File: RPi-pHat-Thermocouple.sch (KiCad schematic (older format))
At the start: 27 parts, among them J1 RPi_GPIO, P1 CONN_01X02, P2 CONN_01X02, P3 CONN_01X02, P4 CONN_01X02, P6 CONN_01X03, Q1 NUD3124, SW1 Write, U1 MAX31850K, U3 MAX31850K, U4 MAX31850K, U5 AT24CS32, U6 MAX31850K

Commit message: Updated schematic parts fields on MAX31850k parts.
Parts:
- U1, U3, U4, U6: Manufacturer (none) -> Maxim; Part Number (none) -> MAX31850KATB+; Vendor (none) -> Mouser; Vendor Part Number (none) -> 700-MAX31850KATB+
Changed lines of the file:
@@
 F 1 "MAX31850K" H 4050 2050 50  0000 L CNN
 F 2 "Housings_DFN_QFN_ML:TDFN-10-1EP_3x4mm_Pitch0.5mm" H 4000 1700 50  0001 C CIN
-F 3 "" H 4000 1700 50  0000 C CNN
+F 3 "https://datasheets.maximintegrated.com/en/ds/MAX31850-MAX31851.pdf" H 4000 1700 50  0001 C CNN
+F 4 "MAX31850KATB+" H 4000 1700 60  0001 C CNN "Part Number"
+F 5 "Maxim" H 4000 1700 60  0001 C CNN "Manufacturer"
+F 6 "Mouser" H 4000 1700 60  0001 C CNN "Vendor"
+F 7 "700-MAX31850KATB+" H 4000 1700 60  0001 C CNN "Vendor Part Number"
 	1    4000 1700
 	1    0    0    -1
@@
 F 1 "MAX31850K" H 4050 3750 50  0000 L CNN
 F 2 "Housings_DFN_QFN_ML:TDFN-10-1EP_3x4mm_Pitch0.5mm" H 4000 3400 50  0001 C CIN
-F 3 "" H 4000 3400 50  0000 C CNN
+F 3 "https://datasheets.maximintegrated.com/en/ds/MAX31850-MAX31851.pdf" H 4000 3400 50  0001 C CNN
+F 4 "MAX31850KATB+" H 4000 3400 60  0001 C CNN "Part Number"
+F 5 "Maxim" H 4000 3400 60  0001 C CNN "Manufacturer"
+F 6 "Mouser" H 4000 3400 60  0001 C CNN "Vendor"
+F 7 "700-MAX31850KATB+" H 4000 3400 60  0001 C CNN "Vendor Part Number"
 	1    4000 3400
 	1    0    0    -1
@@
 F 1 "MAX31850K" H 4050 5450 50  0000 L CNN
 F 2 "Housings_DFN_QFN_ML:TDFN-10-1EP_3x4mm_Pitch0.5mm" H 4000 5100 50  0001 C CIN
-F 3 "" H 4000 5100 50  0000 C CNN
+F 3 "https://datasheets.maximintegrated.com/en/ds/MAX31850-MAX31851.pdf" H 4000 5100 50  0001 C CNN
+F 4 "MAX31850KATB+" H 4000 5100 60  0001 C CNN "Part Number"
+F 5 "Maxim" H 4000 5100 60  0001 C CNN "Manufacturer"
+F 6 "Mouser" H 4000 5100 60  0001 C CNN "Vendor"
+F 7 "700-MAX31850KATB+" H 4000 5100 60  0001 C CNN "Vendor Part Number"
 	1    4000 5100
 	1    0    0    -1
@@
 F 1 "MAX31850K" H 4050 7150 50  0000 L CNN
 F 2 "Housings_DFN_QFN_ML:TDFN-10-1EP_3x4mm_Pitch0.5mm" H 4000 6800 50  0001 C CIN
-F 3 "" H 4000 6800 50  0000 C CNN
+F 3 "https://datasheets.maximintegrated.com/en/ds/MAX31850-MAX31851.pdf" H 4000 6800 50  0001 C CNN
+F 4 "MAX31850KATB+" H 4000 6800 60  0001 C CNN "Part Number"
+F 5 "Maxim" H 4000 6800 60  0001 C CNN "Manufacturer"
+F 6 "Mouser" H 4000 6800 60  0001 C CNN "Vendor"
+F 7 "700-MAX31850KATB+" H 4000 6800 60  0001 C CNN "Vendor Part Number"
 	1    4000 6800
 	1    0    0    -1
@@
 	7050 4000 7050 5450
 Wire Wire Line
-	7050 4000 9600 4000
+	9600 4000 7050 4000
 Wire Wire Line
 	3400 1200 3300 1200

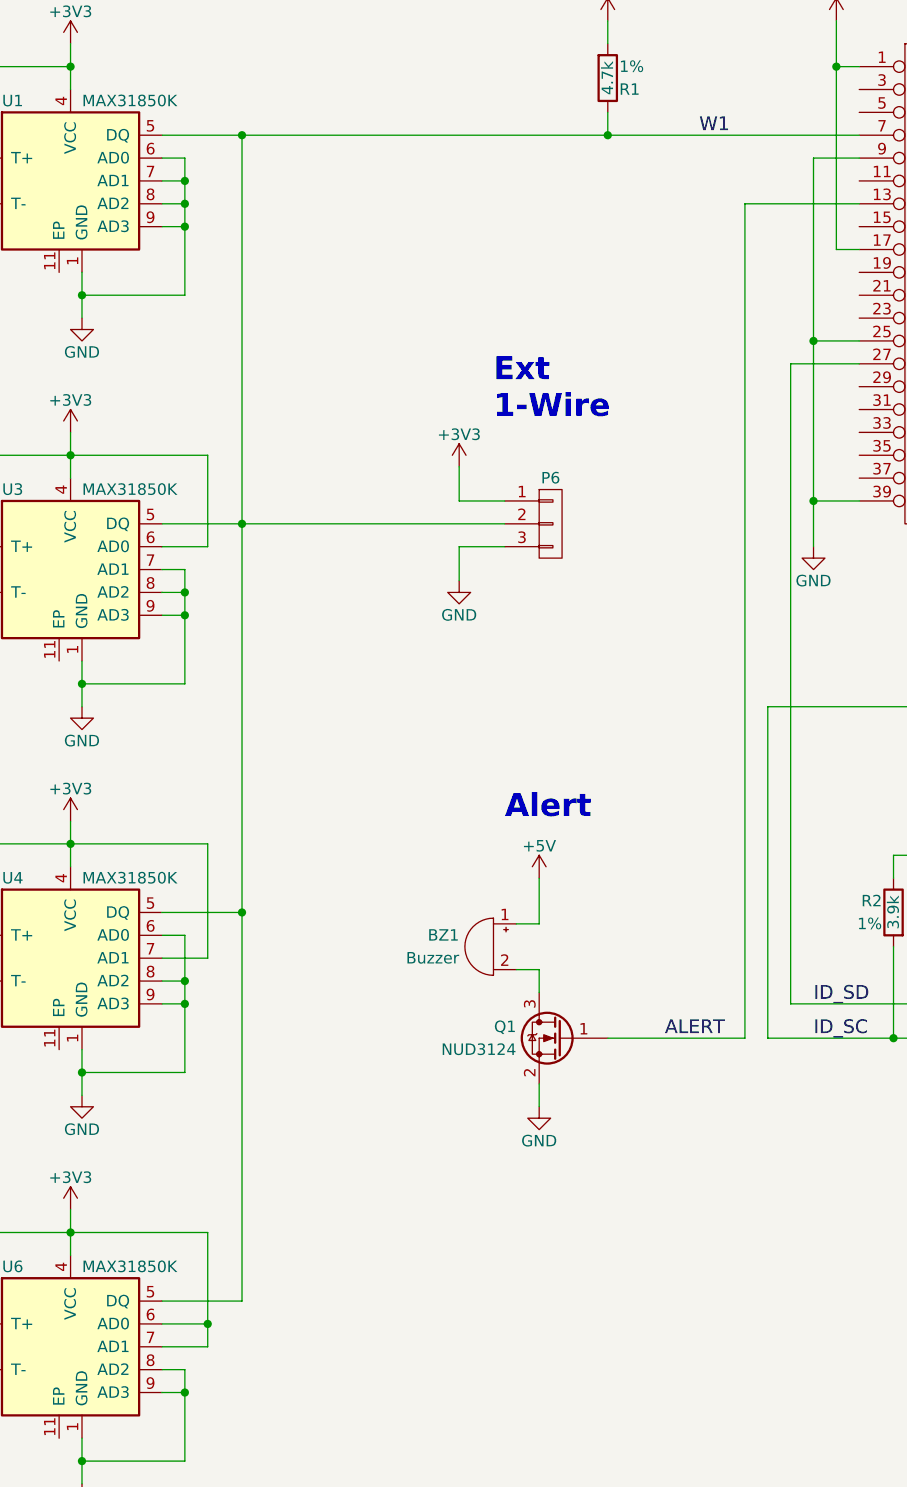
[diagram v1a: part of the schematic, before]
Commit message: Added U2 and R5
Fixed Alert sounding as soon as power is applied by adding pulldown
(R5). Added Ds18S20 (U2) so the Linux kernel will properly access the
MAX31850K.
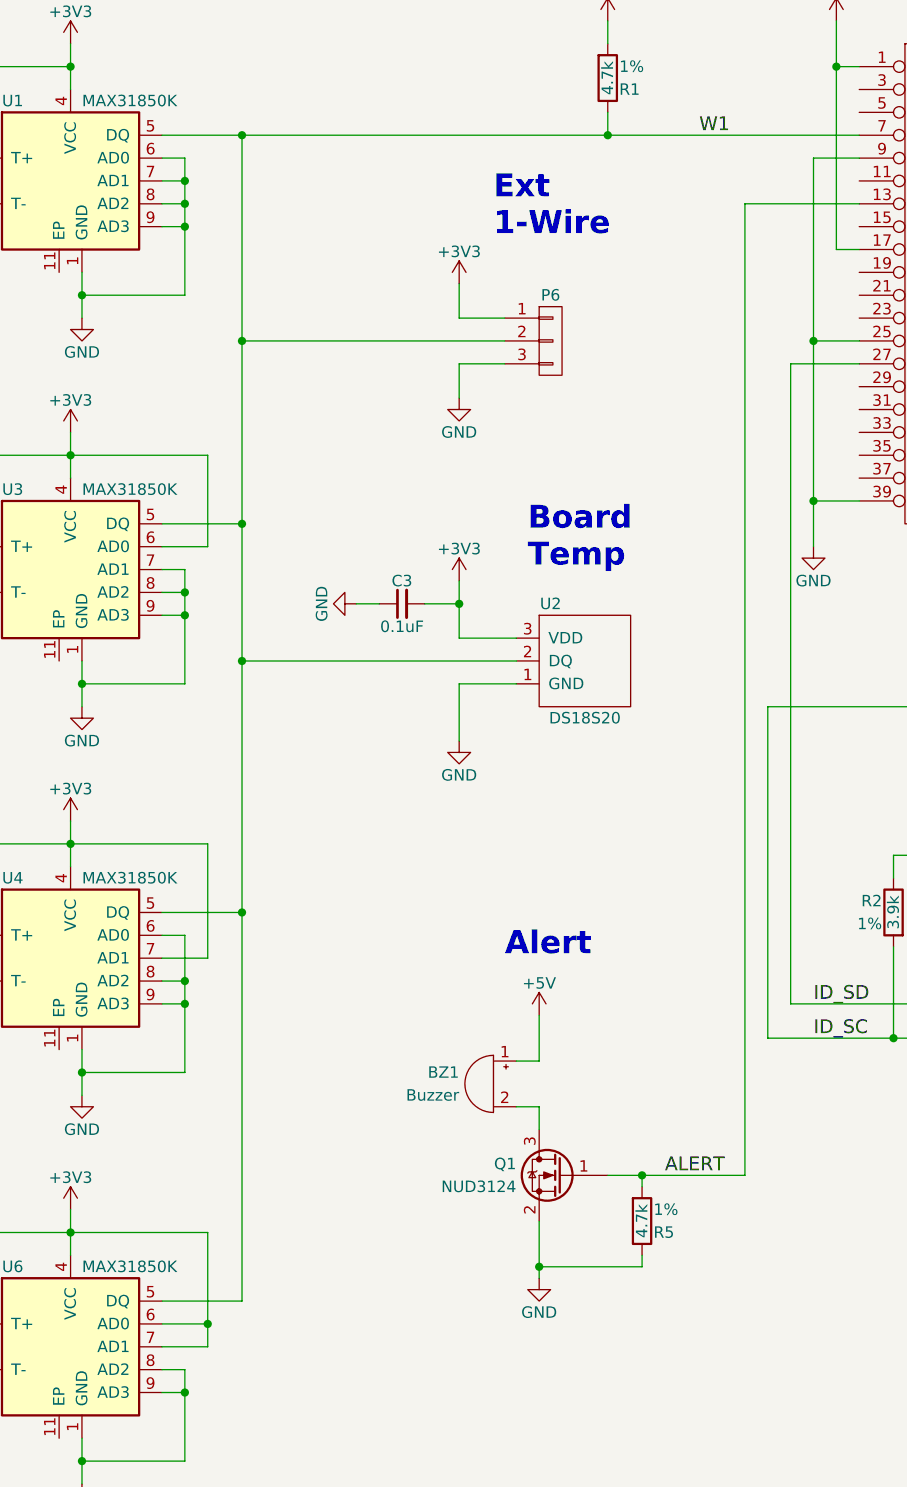
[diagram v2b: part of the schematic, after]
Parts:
- added C3: 0.1uF, Capacitors_SMD:C_0603, symbol C_Small
- added R5: 4.7k, Resistors_SMD:R_0603, symbol R
- added U2: DS18S20, TO_SOT_Packages_THT:TO-92_Molded_Narrow, symbol DS18S20
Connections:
- net +3V3: now also C3.2, U2.3 (VDD)
- net ALERT: now also R5.2
- net GND: now also C3.1, R5.1, U2.1 (GND)
- net W1: now also U2.2 (DQ)
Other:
- note added: "Board\nTemp"
- moved on the sheet: BZ1, P6, Q1

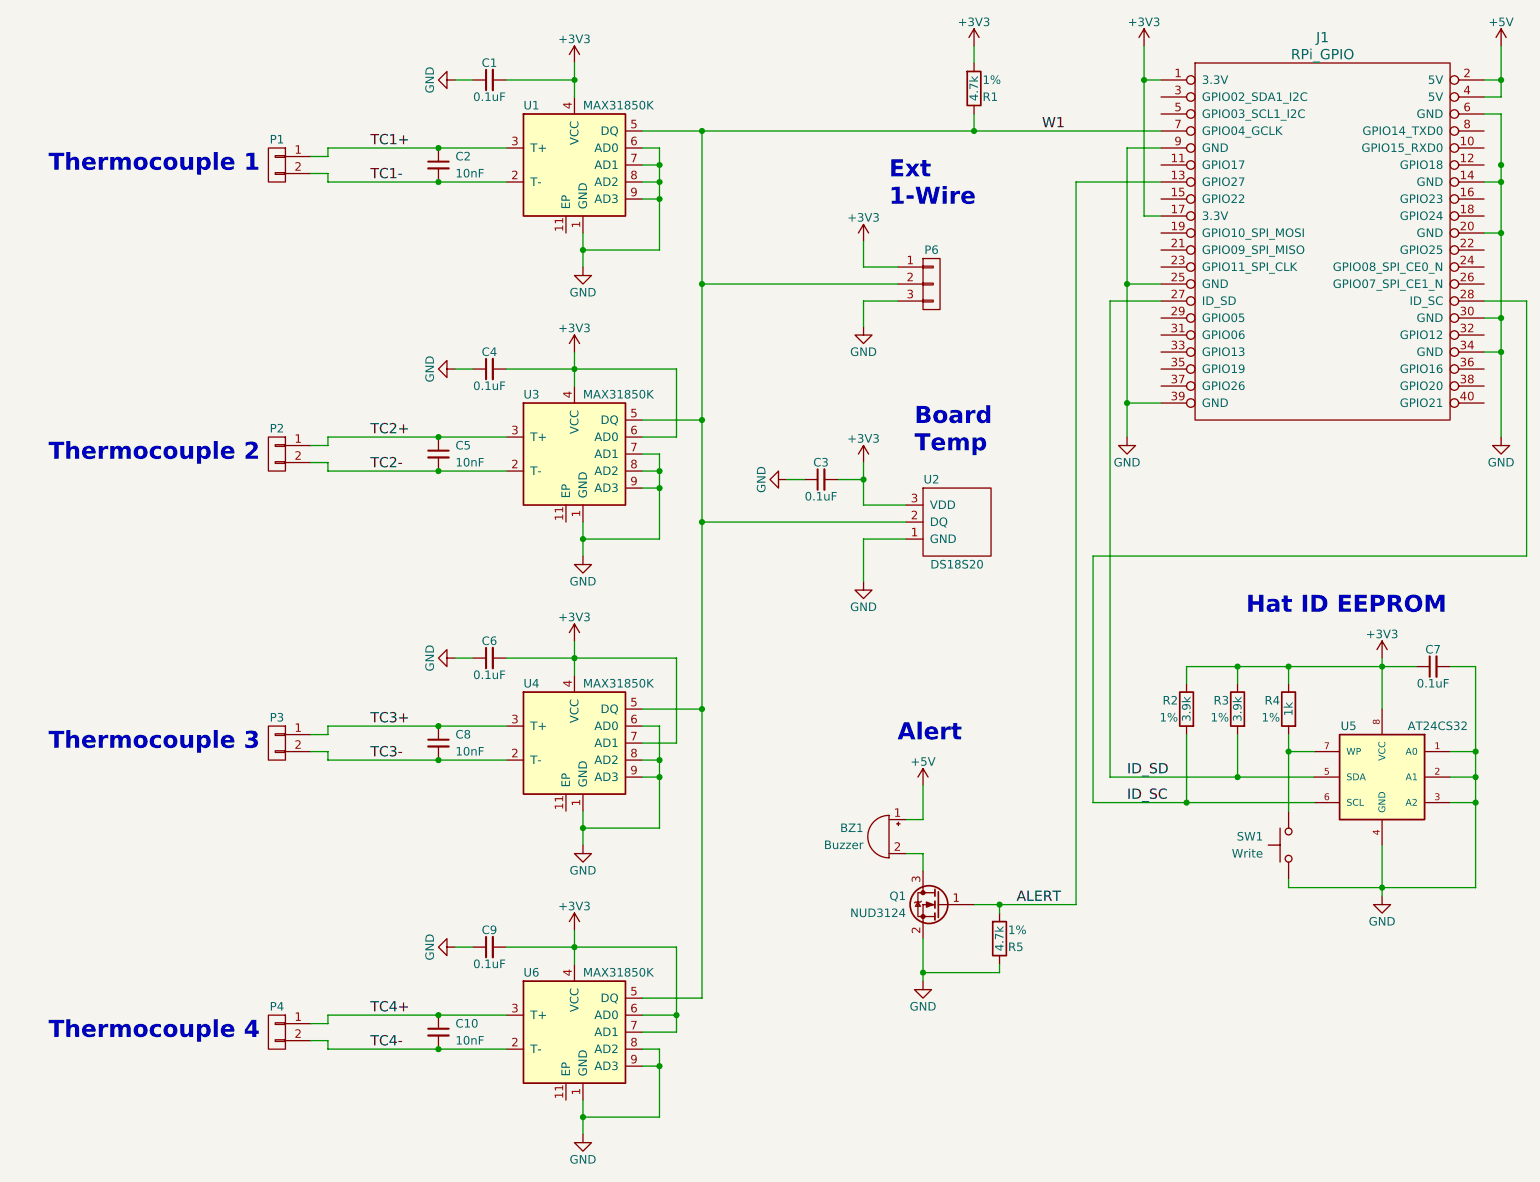
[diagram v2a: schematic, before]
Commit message: Added Analog Power Supply
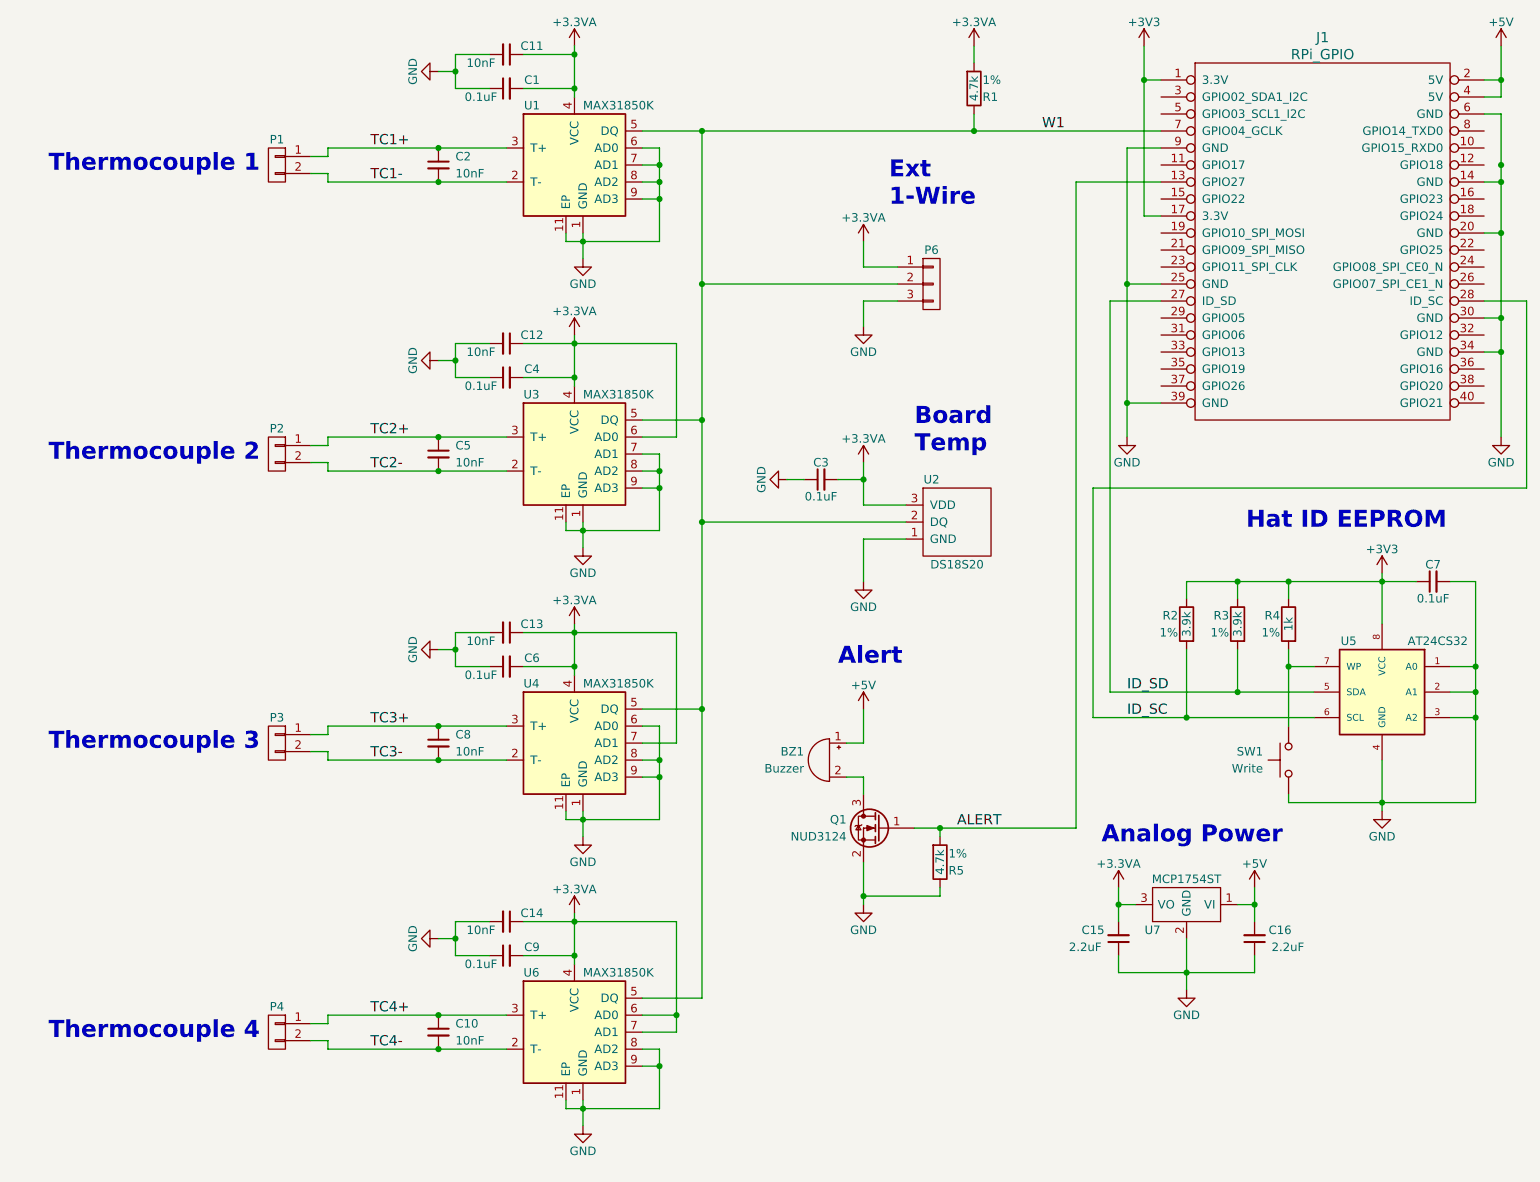
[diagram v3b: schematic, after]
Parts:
- added C11, C12, C13, C14: 10nF, Capacitors_SMD:C_0603, symbol C_Small
- added C15, C16: 2.2uF, Capacitors_SMD:C_0805, symbol C_Small
- added U7: MCP1754ST, TO_SOT_Packages_SMD:SOT89-3_Housing, symbol MCP1754ST-3302E/MB
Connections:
- net +3V3: no longer C1.2, C3.2, C4.2, C6.2, C9.2, P6.1 (P1), R1.2, U1.4 (VCC), U2.3 (VDD), U3.4 (VCC), U3.6 (AD0), U4.4 (VCC), U4.7 (AD1), U6.4 (VCC), U6.6 (AD0), U6.7 (AD1)
- net +5V: now also C16.2, U7.1 (VI)
- net GND: now also U1.11 (EP), U3.11 (EP), U4.11 (EP), U6.11 (EP), C11.2, C12.2, C13.2, C14.2, C15.1, C16.1, U7.2 (GND)
- new net +3.3VA: C1.2, C11.1, C12.1, C13.1, C14.1, C15.2, C3.2, C4.2, C6.2, C9.2, P6.1 (P1), R1.2, U1.4 (VCC), U2.3 (VDD), U3.4 (VCC), U3.6 (AD0), U4.4 (VCC), U4.7 (AD1), U6.4 (VCC), U6.6 (AD0), U6.7 (AD1), U7.3 (VO)
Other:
- note added: "Analog Power"
- moved on the sheet: BZ1, C1, C4, C6, C7, C9, Q1, R2, R3, R4, R5, SW1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
